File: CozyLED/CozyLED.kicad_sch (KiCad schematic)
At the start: 14 parts

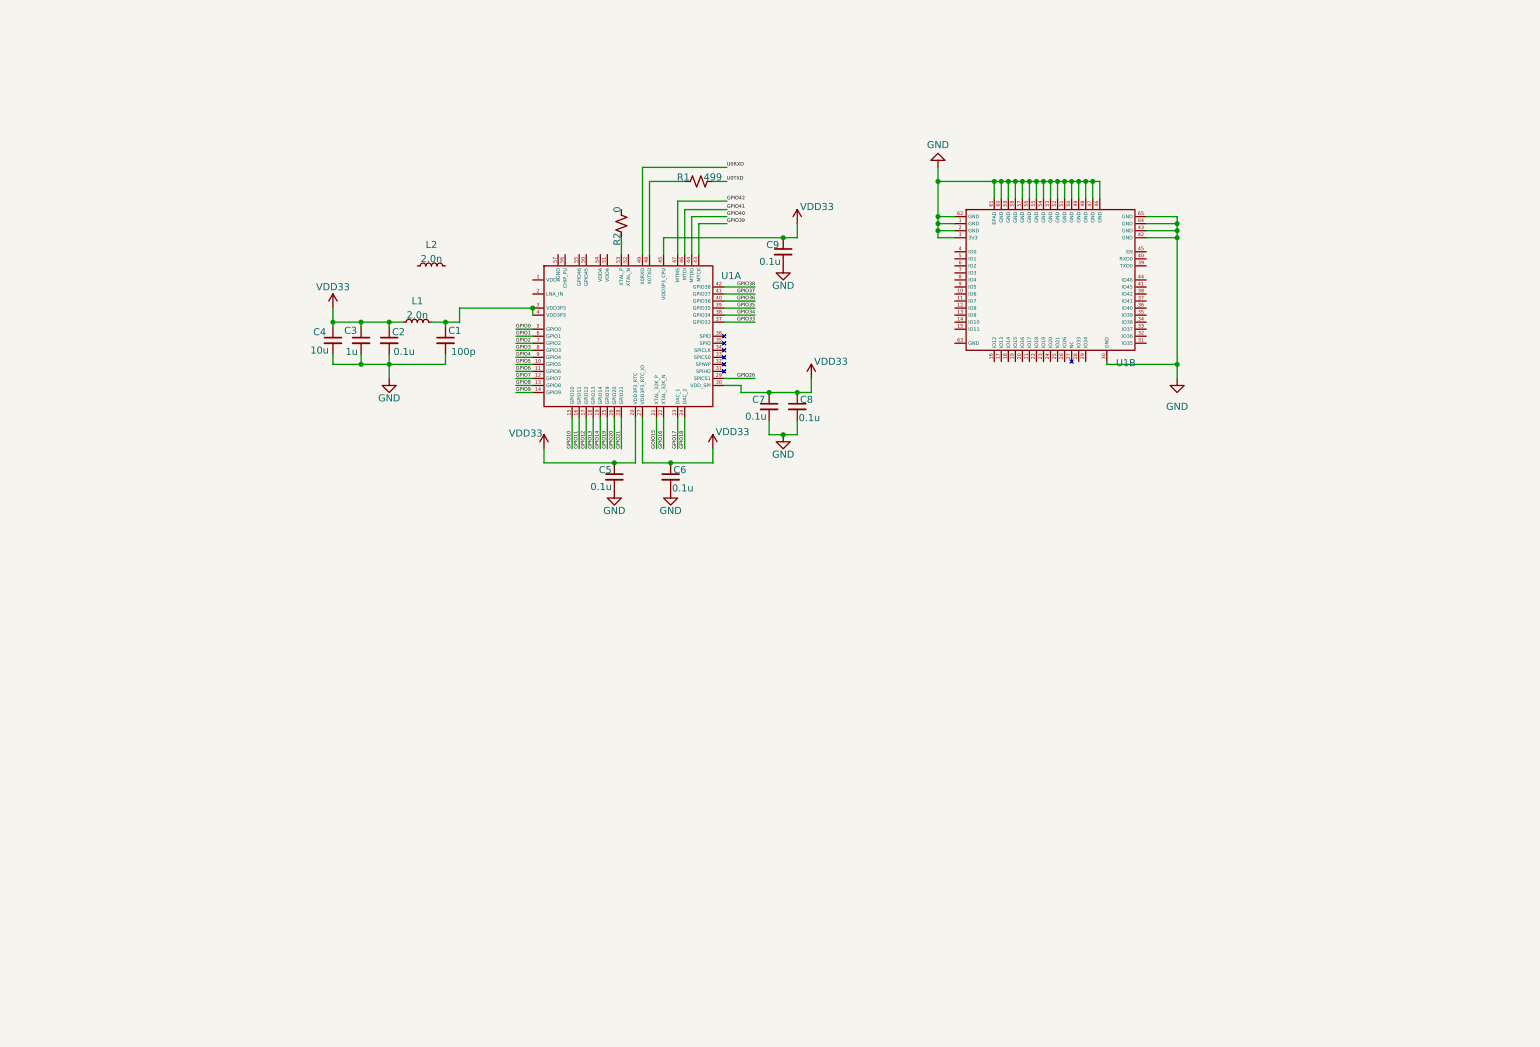
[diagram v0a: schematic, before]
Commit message: Updated CozyLED
+ Adjusted footprint of ESP32 to account for ground pins at center
+ Adjusted ESP32 MINI 2 footprint to account only for peripheral GPIO
+ Updated MOSFETs to control grounding of LED strips
+ Updated LED strip to be based off 12V instead of 5V
+ Laid out board and component placement on 2 layers
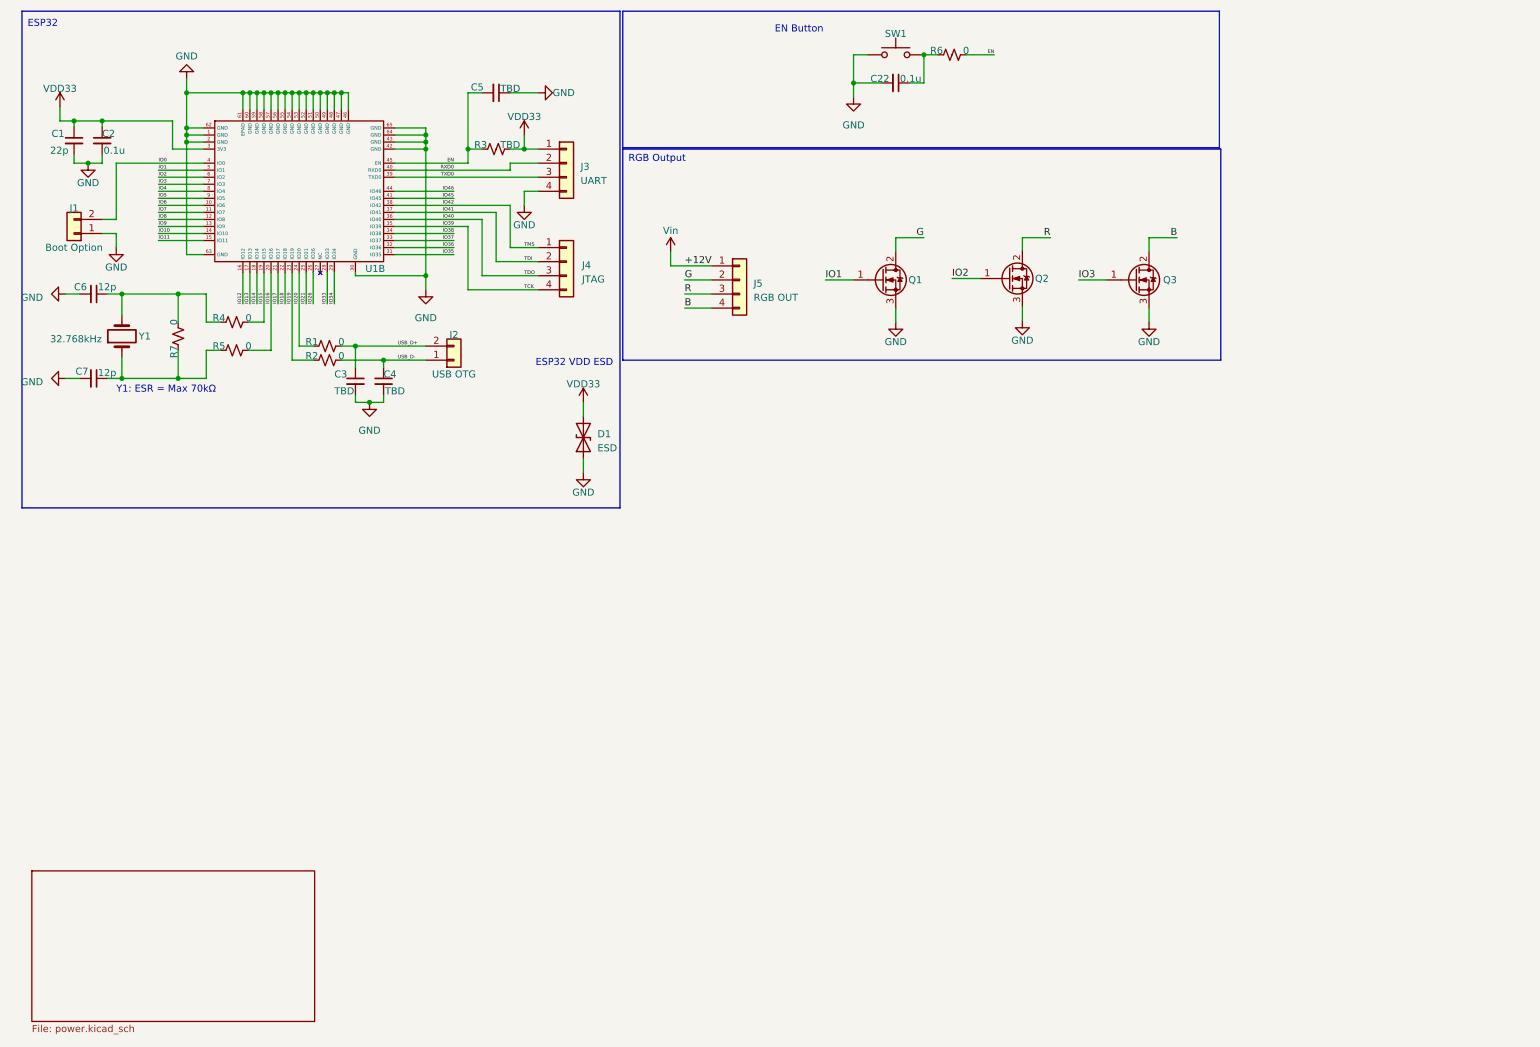
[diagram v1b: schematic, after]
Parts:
- removed C8, C9: 0.1u, symbol Device:C_Small
- removed L1, L2: 2.0n, symbol Device:L_Small
- removed unit 1 of U1
- added C22: 0.1u, Capacitor_SMD:C_0603_1608Metric, symbol Device:C_Small
- added D1: ESD, Diode_SMD:D_SMB, symbol Device:D_TVS
- added J1: Boot Option, Connector_PinHeader_2.00mm:PinHeader_1x02_P2.00mm_Vertical, symbol Connector_Generic:Conn_01x02
- added J2: USB OTG, Connector_PinHeader_2.00mm:PinHeader_1x02_P2.00mm_Vertical, symbol Connector_Generic:Conn_01x02
- added J3: UART, Connector_PinHeader_2.00mm:PinHeader_1x04_P2.00mm_Vertical, symbol Connector_Generic:Conn_01x04
- added J4: JTAG, Connector_PinHeader_2.00mm:PinHeader_1x04_P2.00mm_Vertical, symbol Connector_Generic:Conn_01x04
- added J5: RGB OUT, Connector_PinHeader_2.00mm:PinHeader_1x04_P2.00mm_Horizontal, symbol Connector_Generic:Conn_01x04
- added Q1, Q2, Q3: Q_NMOS_GDS, Diodes INC:DMN1019USN_N_CHNL, symbol Device:Q_NMOS_GDS
- added R3: TBD, Resistor_SMD:R_0402_1005Metric, symbol Device:R_Small_US
- added R4, R5, R6, R7: 0, Resistor_SMD:R_0402_1005Metric, symbol Device:R_Small_US
- added SW1: SW_Push, Button_Switch_THT:SW_PUSH_6mm, symbol Switch:SW_Push
- added Y1: 32.768kHz, Crystal:Crystal_SMD_3215-2Pin_3.2x1.5mm, symbol Device:Crystal
- C1: value 100p -> 22p; footprint (none) -> Capacitor_SMD:C_0402_1005Metric
- C2: footprint (none) -> Capacitor_SMD:C_0603_1608Metric
- C3: value 1u -> TBD; footprint (none) -> Capacitor_SMD:C_0603_1608Metric
- C4: value 10u -> TBD; footprint (none) -> Capacitor_SMD:C_0603_1608Metric
- C5: value 0.1u -> TBD; footprint (none) -> Capacitor_SMD:C_0603_1608Metric
- C6, C7: value 0.1u -> 12p; footprint (none) -> Capacitor_SMD:C_0603_1608Metric
- R1: value 499 -> 0; footprint (none) -> Resistor_SMD:R_0402_1005Metric
- R2: footprint (none) -> Resistor_SMD:R_0402_1005Metric
- U1: footprint (none) -> ESP32:ESP32_S2_MINI_2
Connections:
- net +3V3: now also C1.1, U1.3 (3V3), D1.2 (A2), J3.1 (Pin_1), R3.2; no longer C3.1, C4.1, C5.1, C6.1, C7.1
- net GND: now also C5.1, U1.63 (GND), C22.2, D1.1 (A1), J1.1 (Pin_1), J3.4 (Pin_4), Q1.3 (S), Q2.3 (S), Q3.3 (S), SW1.1; no longer C5.2, U1.3 (3V3)
- net IO19: now reaches R2.1
- net IO19: now also U1.23 (IO19)
- net USB_D-: now reaches R2.2
- net USB_D-: now also C4.1, J2.1 (Pin_1)
- net IO20: now reaches R1.1
- net IO20: now also U1.24 (IO20)
- net IO6: now reaches U1.10 (IO6)
- net IO7: now reaches U1.11 (IO7)
- net IO8: now reaches U1.12 (IO8)
- net IO9: now reaches U1.13 (IO9)
- net IO10: now reaches U1.14 (IO10)
- net IO11: now reaches U1.15 (IO11)
- net IO12: now reaches U1.16 (IO12)
- net IO13: now reaches U1.17 (IO13)
- net IO14: now reaches U1.18 (IO14)
- net IO15: now reaches U1.19 (IO15)
- net IO15: now also R4.2
- net IO16: now reaches U1.20 (IO16)
- net IO16: now also R5.2
- net IO17: now reaches U1.21 (IO17)
- net IO18: now reaches U1.22 (IO18)
- net IO21: now reaches U1.25 (IO21)
- net IO26: now reaches U1.26 (IO26)
- net IO33: now reaches U1.28 (IO33)
- net IO34: now reaches U1.29 (IO34)
- net IO35: now reaches U1.31 (IO35)
- net IO36: now reaches U1.32 (IO36)
- net IO37: now reaches U1.33 (IO37)
- net IO38: now reaches U1.34 (IO38)
- net IO39: now reaches U1.35 (IO39)
- net IO39: now also J4.4 (Pin_4)
- net IO40: now reaches U1.36 (IO40)
- net IO40: now also J4.3 (Pin_3)
- net IO41: now reaches U1.37 (IO41)
- net IO41: now also J4.2 (Pin_2)
- net IO42: now reaches U1.38 (IO42)
- net IO42: now also J4.1 (Pin_1)
- net TXD0: now reaches U1.39 (TXD0)
- net TXD0: now also J3.3 (Pin_3)
- net IO0: now reaches U1.4 (IO0)
- net IO0: now also J1.2 (Pin_2)
- net RXD0: now reaches U1.40 (RXD0)
- net RXD0: now also J3.2 (Pin_2)
- net IO45: now reaches U1.41 (IO45)
- net IO46: now reaches U1.44 (IO46)
- net EN: now reaches U1.45 (EN)
- net EN: now also C5.2, R3.1, R6.2
- net IO1: now reaches U1.5 (IO1)
- net IO1: now also Q1.1 (G)
- net IO2: now reaches U1.6 (IO2)
- net IO2: now also Q2.1 (G)
- net IO3: now reaches U1.7 (IO3)
- net IO3: now also Q3.1 (G)
- net IO4: now reaches U1.8 (IO4)
- net IO5: now reaches U1.9 (IO5)
- net U0TXD renamed USB_D+
- net USB_D+: now also C3.1, J2.2 (Pin_2)
- new net: C22.1, R6.1, SW1.2
- new net: C7.1, R5.1, R7.1, Y1.1
- new net: C6.1, R4.1, R7.2, Y1.2
- new net B: J5.4 (Pin_4), Q3.2 (D)
- new net G: J5.2 (Pin_2), Q1.2 (D)
- new net R: J5.3 (Pin_3), Q2.2 (D)
- new net VCC: J5.1 (Pin_1)
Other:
- added sheet Power (power.kicad_sch)
- note added: "EN Button"
- note added: "ESP32"
- note added: "ESP32 VDD ESD"
- note added: "RGB Output"
- note added: "Y1: ESR = Max 70kΩ"
- title: (none) -> CozyLED

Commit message: Updated v0.1
- Added documentation
- Designed initial state machine
- Tested state machine to correctly initialize then enter default
- Added initial LED code for static color
- Added initial LED code for breathing color
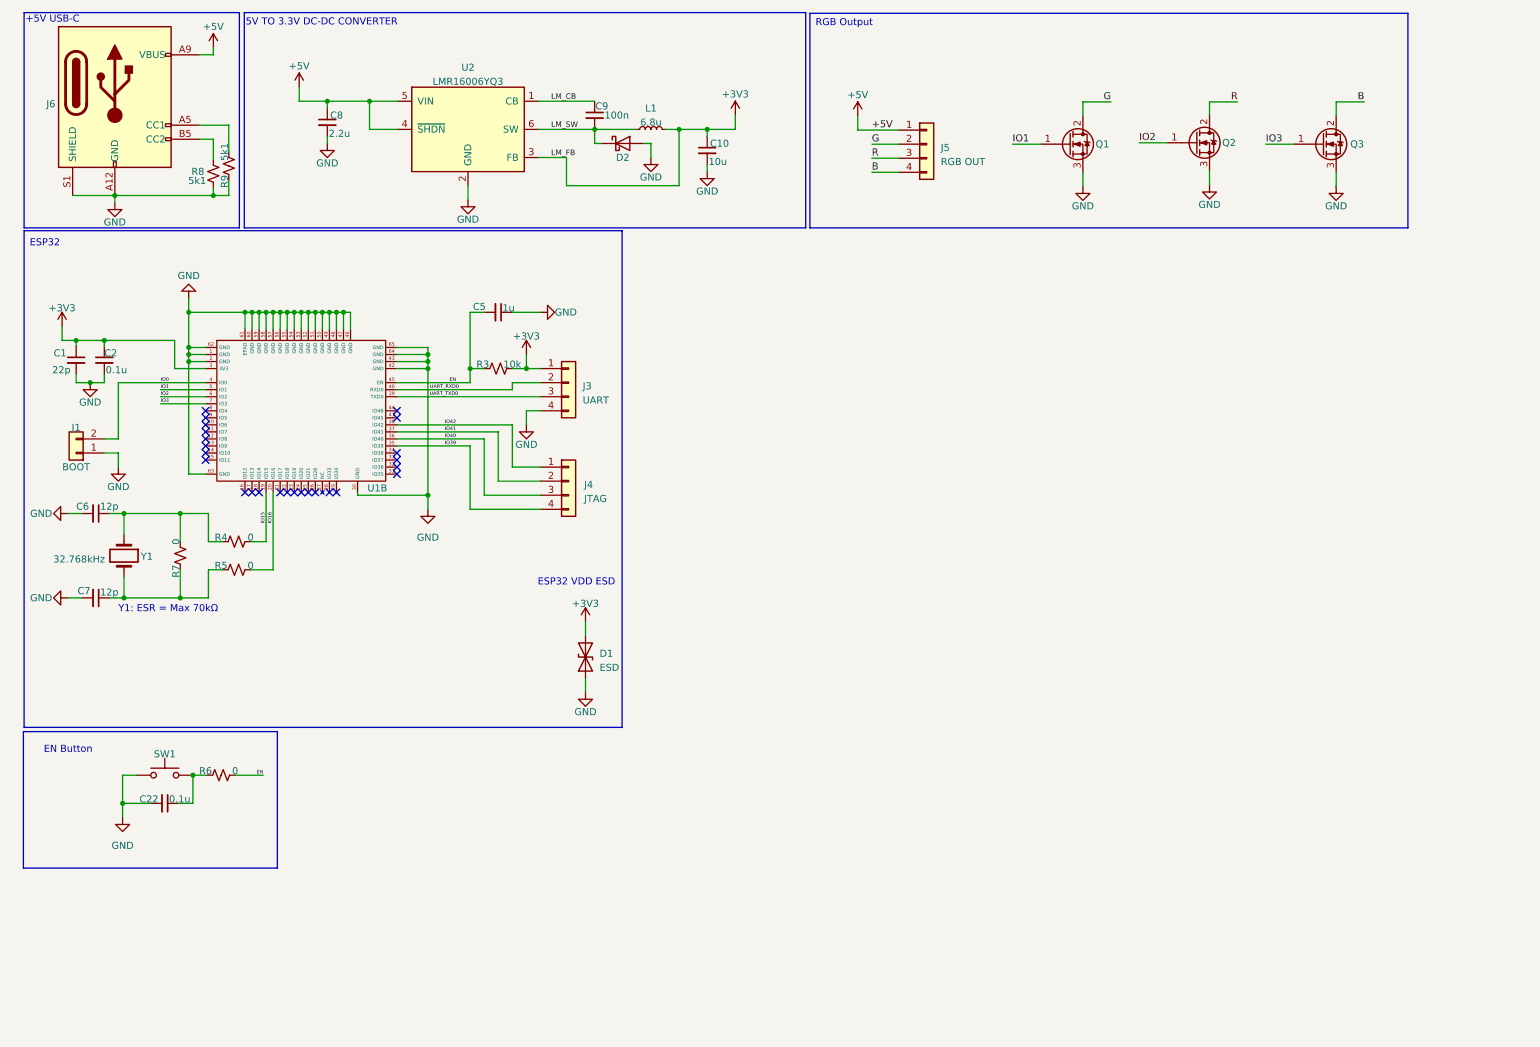
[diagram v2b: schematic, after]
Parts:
- removed C3, C4: TBD, Capacitor_SMD:C_0603_1608Metric, symbol Device:C_Small
- removed J2: USB OTG, Connector_PinHeader_2.00mm:PinHeader_1x02_P2.00mm_Vertical, symbol Connector_Generic:Conn_01x02
- removed R1, R2: 0, Resistor_SMD:R_0402_1005Metric, symbol Device:R_Small_US
- added C10: 10u, Capacitor_SMD:C_0805_2012Metric, symbol Device:C_Small
- added C8: 2.2u, Capacitor_SMD:C_0603_1608Metric, symbol Device:C_Small
- added C9: 100n, Capacitor_SMD:C_0402_1005Metric, symbol Device:C_Small
- added D2: D_Schottky, Diode_SMD:D_0603_1608Metric, symbol Device:D_Schottky
- added J6: USB_C_Receptacle_PowerOnly_6P, Connector_USB:USB_C_Receptacle_GCT_USB4135-GF-A_6P_TopMnt_Horizontal, symbol Connector:USB_C_Receptacle_PowerOnly_6P
- added L1: 6.8u, Inductor_SMD:L_6.3x6.3_H3, symbol Device:L_Small
- added R8, R9: 5k1, Resistor_SMD:R_0402_1005Metric, symbol Device:R_Small_US
- added U2: LMR16006YQ3, Package_TO_SOT_SMD:SOT-23-6, symbol Regulator_Switching:LMR16006YQ3
- C1: footprint Capacitor_SMD:C_0402_1005Metric -> Capacitor_SMD:C_0603_1608Metric
- C2, C22, C6, C7: footprint Capacitor_SMD:C_0603_1608Metric -> Capacitor_SMD:C_0402_1005Metric
- C5: value TBD -> 1u
- J1: value Boot Option -> BOOT
- J5: footprint Connector_PinHeader_2.00mm:PinHeader_1x04_P2.00mm_Horizontal -> Connector_JST:JST_EH_S4B-EH_1x04_P2.50mm_Horizontal
- R3: value TBD -> 10k
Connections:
- net +3V3: now also C10.1, L1.2, U2.3 (FB)
- net GND: now also C10.2, C8.2, D2.2 (A), J6.A12 (GND), J6.B12 (GND), J6.S1 (SHIELD), R8.1, R9.1, U2.2 (GND)
- net at C7.1, R5.1, R7.1: now also Y1.2; no longer Y1.1
- net at C6.1, R4.1, R7.2: now also Y1.1; no longer Y1.2
- net IO10: no longer names the net of U1.14 (IO10)
- net IO11: no longer names the net of U1.15 (IO11)
- net IO12: no longer names the net of U1.16 (IO12)
- net IO13: no longer names the net of U1.17 (IO13)
- net IO14: no longer names the net of U1.18 (IO14)
- net IO17: no longer names the net of U1.21 (IO17)
- net IO18: no longer names the net of U1.22 (IO18)
- net IO19: no longer names the net of U1.23 (IO19)
- net IO20: no longer names the net of U1.24 (IO20)
- net IO21: no longer names the net of U1.25 (IO21)
- net IO26: no longer names the net of U1.26 (IO26)
- net IO33: no longer names the net of U1.28 (IO33)
- net IO34: no longer names the net of U1.29 (IO34)
- net IO35: no longer names the net of U1.31 (IO35)
- net IO36: no longer names the net of U1.32 (IO36)
- net IO37: no longer names the net of U1.33 (IO37)
- net IO38: no longer names the net of U1.34 (IO38)
- net IO4: no longer names the net of U1.8 (IO4)
- net IO45: no longer names the net of U1.41 (IO45)
- net IO46: no longer names the net of U1.44 (IO46)
- net IO5: no longer names the net of U1.9 (IO5)
- net IO6: no longer names the net of U1.10 (IO6)
- net IO7: no longer names the net of U1.11 (IO7)
- net IO8: no longer names the net of U1.12 (IO8)
- net IO9: no longer names the net of U1.13 (IO9)
- net RXD0 renamed UART_RXD0
- net TXD0 renamed UART_TXD0
- net VCC renamed +5V
- net +5V: now also C8.1, J6.A9 (VBUS), J6.B9 (VBUS), U2.4 (~{SHDN}), U2.5 (VIN)
- new net: J6.A5 (CC1), R9.2
- new net: J6.B5 (CC2), R8.2
- new net LM_CB: C9.1, U2.1 (CB)
- new net LM_SW: C9.2, D2.1 (K), L1.1, U2.6 (SW)
- no-connect marks 0 -> 25
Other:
- removed sheet Power
- note added: "+5V USB-C"
- note added: "5V TO 3.3V DC-DC CONVERTER"
- moved on the sheet: C1, C2, C22, C5, C6, C7, D1, J1, J3, J4, J5, Q1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
